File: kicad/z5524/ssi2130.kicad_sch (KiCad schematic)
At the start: 47 parts, among them Q1 2N7002K, U16 SSI2130, U17 DG442xY, U18 TL072, U19 LM311

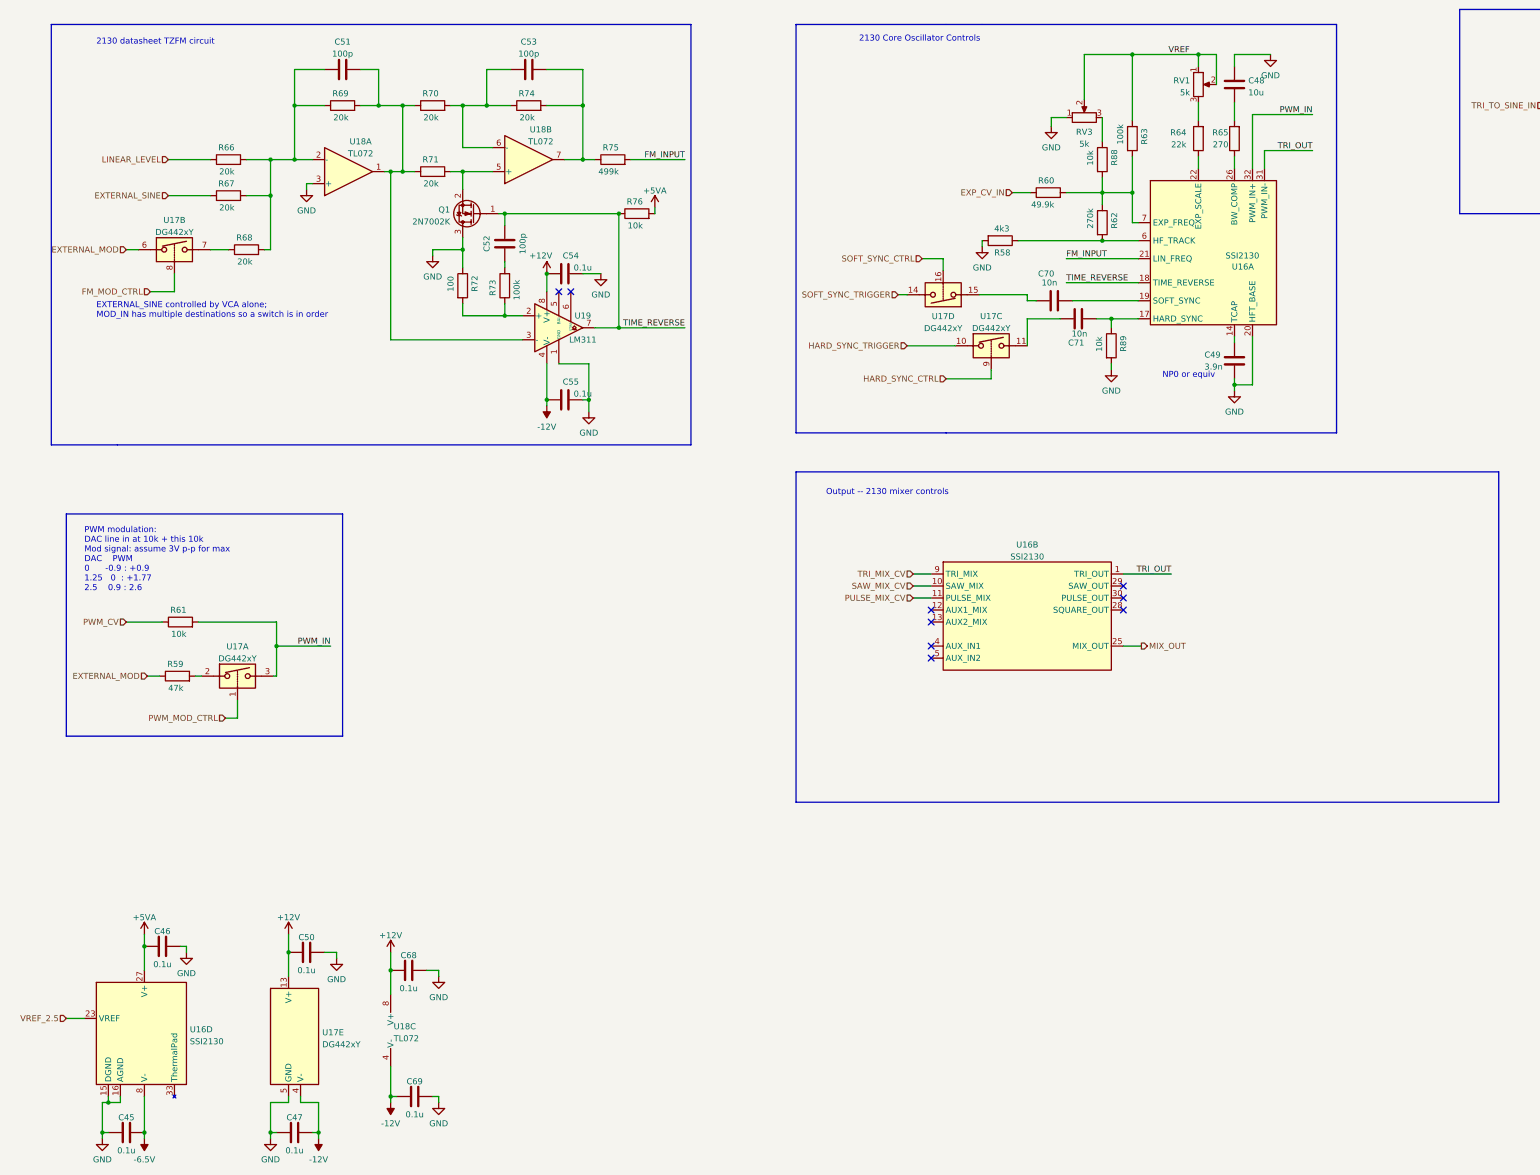
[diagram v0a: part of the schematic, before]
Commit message: calc Vref resistors and fix a couple errors
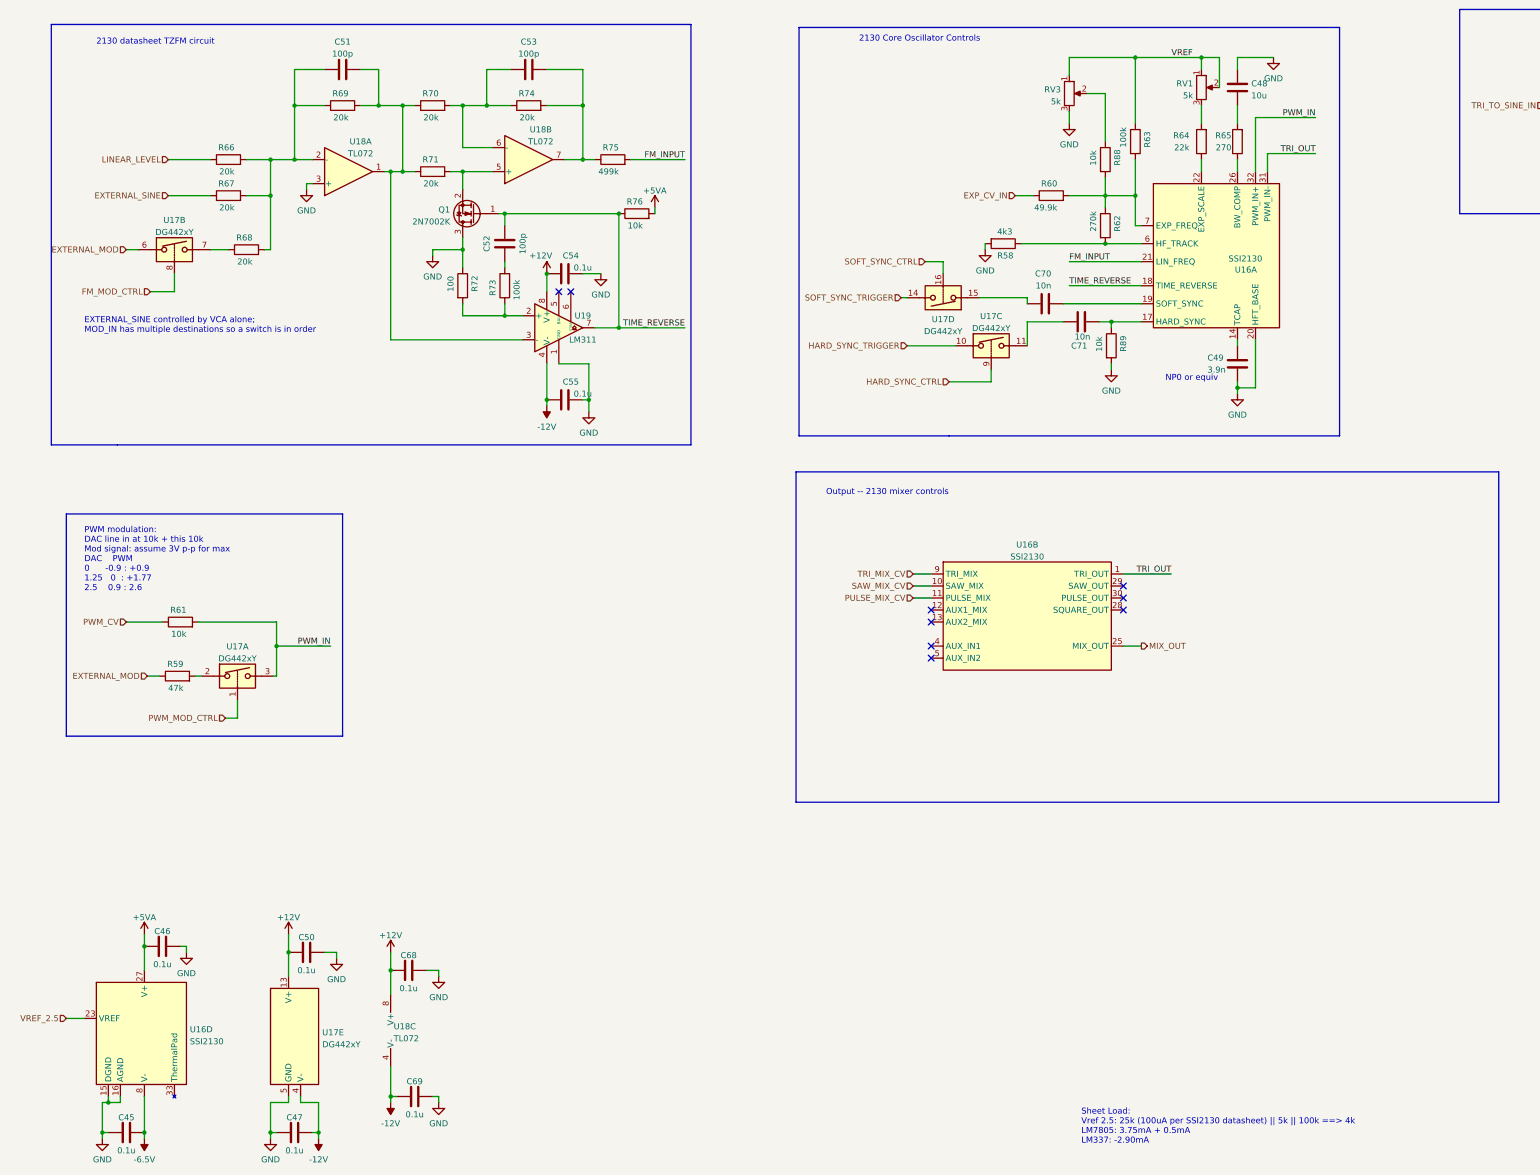
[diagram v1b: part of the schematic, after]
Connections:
- net GND: now also RV3.3; no longer RV3.1
- net VREF: now also RV3.1; no longer RV3.2
- net at R88.1: now also RV3.2; no longer RV3.3
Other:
- note added: "Sheet Load: Vref 2.5: 25k (100uA per SSI2130 datasheet) || 5k || 100k ==> 4k LM7805: 3.75mA + 0.5mA LM337: -2.90mA"
- moved on the sheet: C48, C49, C70, C71, R58, R60, R62, R63, R64, R65, R88, RV1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

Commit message: modify footprint; modify some schematic values
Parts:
- U16: footprint Package_DFN_QFN:QFN-32-1EP_4x4mm_P0.4mm_EP2.65x2.65mm -> Package_DFN_QFN:QFN-32-1EP_4x4mm_P0.4mm_EP2.65x2.65mm_Handsolder
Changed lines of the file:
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@@
     (property "Reference" "U16" (id 0) (at 227.33 127.161 0))
     (property "Value" "SSI2130" (id 1) (at 227.33 129.6979 0))
-    (property "Footprint" "Package_DFN_QFN:QFN-32-1EP_4x4mm_P0.4mm_EP2.65x2.65mm" (id 2) (at 227.33 135.89 0)
+    (property "Footprint" "Package_DFN_QFN:QFN-32-1EP_4x4mm_P0.4mm_EP2.65x2.65mm_Handsolder" (id 2) (at 227.33 135.89 0)
       (effects (font (size 1.27 1.27)) hide)
     )
@@
       (effects (font (size 1.27 1.27)) (justify left))
     )
-    (property "Footprint" "Package_DFN_QFN:QFN-32-1EP_4x4mm_P0.4mm_EP2.65x2.65mm" (id 2) (at 41.91 226.06 0)
+    (property "Footprint" "Package_DFN_QFN:QFN-32-1EP_4x4mm_P0.4mm_EP2.65x2.65mm_Handsolder" (id 2) (at 41.91 226.06 0)
       (effects (font (size 1.27 1.27)) hide)
     )
@@
       (effects (font (size 1.27 1.27)) (justify left))
     )
-    (property "Footprint" "Package_DFN_QFN:QFN-32-1EP_4x4mm_P0.4mm_EP2.65x2.65mm" (id 2) (at 270.51 63.5 0)
+    (property "Footprint" "Package_DFN_QFN:QFN-32-1EP_4x4mm_P0.4mm_EP2.65x2.65mm_Handsolder" (id 2) (at 270.51 63.5 0)
       (effects (font (size 1.27 1.27)) hide)
     )
@@
     (property "Reference" "U16" (id 0) (at 383.54 26.831 0))
     (property "Value" "SSI2130" (id 1) (at 383.54 29.3679 0))
-    (property "Footprint" "Package_DFN_QFN:QFN-32-1EP_4x4mm_P0.4mm_EP2.65x2.65mm" (id 2) (at 384.175 38.1 0)
-      (effects (font (size 1.27 1.27)) hide)
-    )
+    (property "Footprint" "Package_DFN_QFN:QFN-32-1EP_4x4mm_P0.4mm_EP2.65x2.65mm_Handsolder" (id 2) (at 384.175 38.1 0)
+      (effects (font (size 1.27 1.27)) hide)
+    )

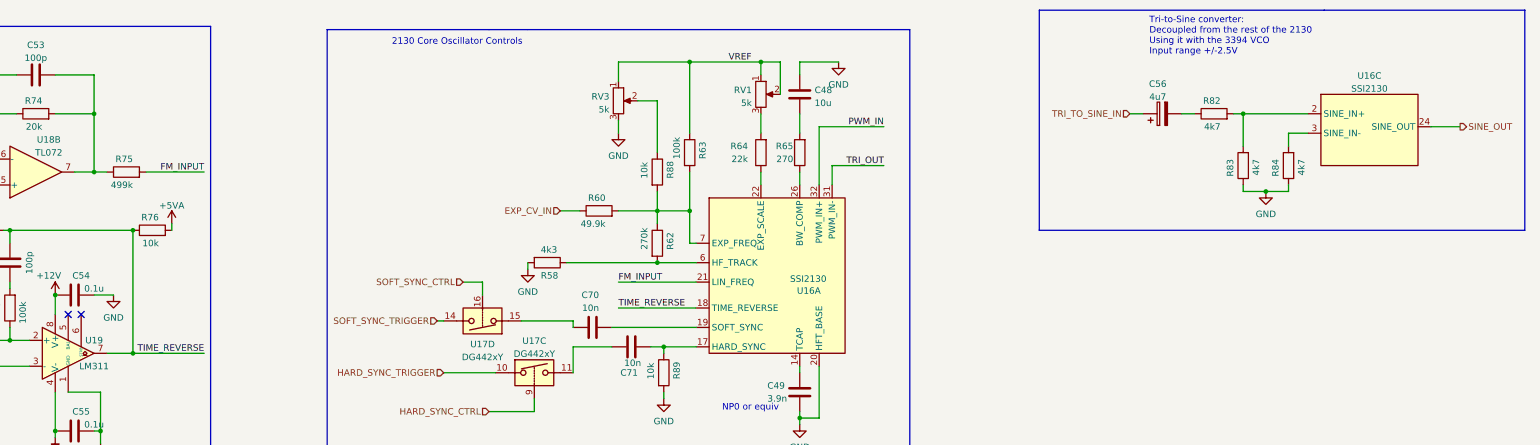
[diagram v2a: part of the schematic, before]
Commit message: further footprint mods; some placement
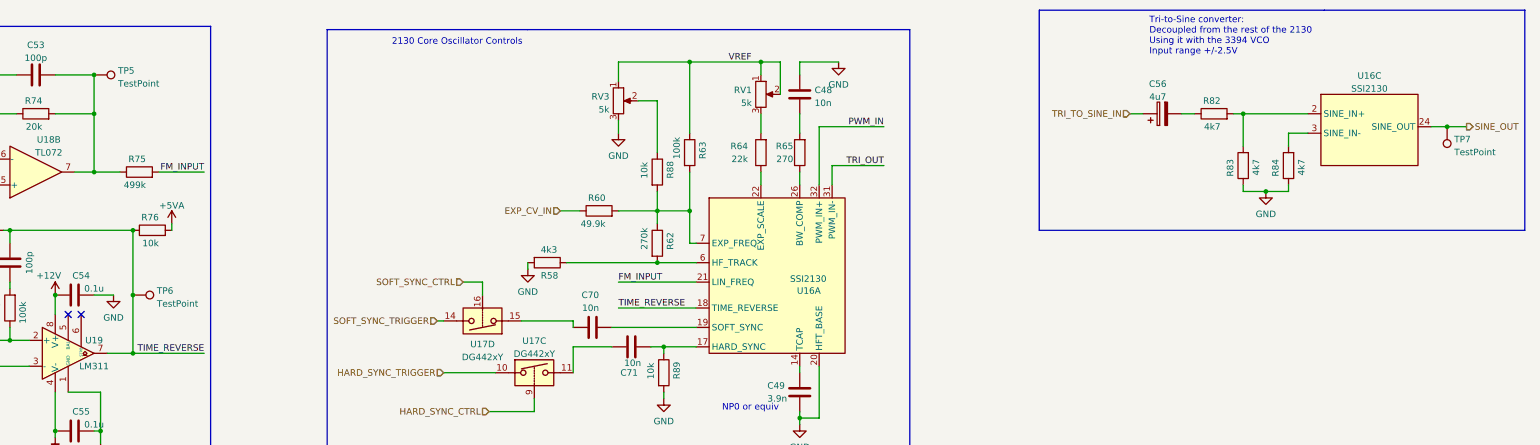
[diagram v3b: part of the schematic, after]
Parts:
- added TP5, TP6, TP7: TestPoint, TestPoint:TestPoint_Pad_1.5x1.5mm, symbol Connector:TestPoint
- C48: value 10u -> 10n; footprint Capacitor_SMD:C_0805_2012Metric -> Capacitor_SMD:C_0603_1608Metric; LCSC Part C15850 -> C57112
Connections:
- net SINE_OUT: now also TP7.1
- net TIME_REVERSE: now also TP6.1
- net at C53.2, R74.2, R75.1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: now also TP5.1
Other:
- moved on the sheet: R75
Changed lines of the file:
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@@
     (company "Zoxnoxious Engineering")
   )
+  (junction (at 398.78 36.83) (diameter 0) (color 0 0 0 0)
+  )
   (junction (at 140.97 57.15) (diameter 0) (color 0 0 0 0)
   )
@@
   (junction (at 92.71 48.26) (diameter 0) (color 0 0 0 0)
   )
+  (junction (at 133.35 26.67) (diameter 0) (color 0 0 0 0)
+  )
   (junction (at 67.31 53.34) (diameter 0) (color 0 0 0 0)
   )
@@
   )
   (junction (at 92.71 243.84) (diameter 0) (color 0 0 0 0)
+  )
+  (junction (at 140.97 69.85) (diameter 0) (color 0 0 0 0)
   )
   (no_connect (at 207.01 151.13))
@@
     (stroke (width 0) (type default) (color 0 0 0 0))
   )
-  (wire (pts (xy 395.605 36.83) (xy 401.32 36.83))
+  (wire (pts (xy 395.605 36.83) (xy 398.78 36.83))
     (stroke (width 0) (type default) (color 0 0 0 0))
   )
@@
     (stroke (width 0) (type default) (color 0 0 0 0))
   )
-  (wire (pts (xy 143.51 45.72) (xy 154.94 45.72))
+  (wire (pts (xy 146.05 45.72) (xy 154.94 45.72))
     (stroke (width 0) (type default) (color 0 0 0 0))
   )
@@
     (stroke (width 0) (type default) (color 0 0 0 0))
   )
+  (wire (pts (xy 140.97 69.85) (xy 140.97 57.15))
+    (stroke (width 0) (type default) (color 0 0 0 0))
+  )
   (wire (pts (xy 107.95 48.26) (xy 107.95 52.07))
     (stroke (width 0) (type default) (color 0 0 0 0))
@@
     (stroke (width 0) (type default) (color 0 0 0 0))
   )
-  (wire (pts (xy 140.97 81.28) (xy 140.97 57.15))
+  (wire (pts (xy 140.97 81.28) (xy 140.97 69.85))
     (stroke (width 0) (type default) (color 0 0 0 0))
   )
@@
     (stroke (width 0) (type default) (color 0 0 0 0))
   )
+  (wire (pts (xy 398.78 36.83) (xy 402.59 36.83))
+    (stroke (width 0) (type default) (color 0 0 0 0))
+  )
   (wire (pts (xy 36.83 64.77) (xy 39.37 64.77))
     (stroke (width 0) (type default) (color 0 0 0 0))
@@
     (stroke (width 0) (type default) (color 0 0 0 0))
   )
-  (wire (pts (xy 133.35 45.72) (xy 135.89 45.72))
-    (stroke (width 0) (type default) (color 0 0 0 0))
-  )
   (wire (pts (xy 74.93 50.8) (xy 74.93 52.07))
     (stroke (width 0) (type default) (color 0 0 0 0))
@@
   )
   (wire (pts (xy 107.95 62.23) (xy 107.95 64.77))
+    (stroke (width 0) (type default) (color 0 0 0 0))
+  )
+  (wire (pts (xy 133.35 45.72) (xy 138.43 45.72))
     (stroke (width 0) (type default) (color 0 0 0 0))
   )
@@
     (effects (font (size 1.27 1.27)) (justify right))
   )
-  (hierarchical_label "SINE_OUT" (shape output) (at 401.32 36.83 0)
+  (hierarchical_label "SINE_OUT" (shape output) (at 402.59 36.83 0)
     (effects (font (size 1.27 1.27)) (justify left))
   )
@@
     (pin "1")
   )
-  (symbol (lib_id "Device:R") (at 139.7 45.72 90) (unit 1)
-    (in_bom yes) (on_board yes)
-    (property "Reference" "R75" (id 0) (at 140.97 43.18 90)
-      (effects (font (size 1.27 1.27)) (justify left))
-    )
-    (property "Value" "499k" (id 1) (at 140.97 48.26 90)
-      (effects (font (size 1.27 1.27)) (justify left))
-    )
-    (property "Footprint" "Resistor_SMD:R_0603_1608Metric" (id 2) (at 139.7 47.498 90)
-      (effects (font (size 1.27 1.27)) hide)
-    )
-    (property "Datasheet" "~" (id 3) (at 139.7 45.72 0)
-      (effects (font (size 1.27 1.27)) hide)
-    )
-    (property "LCSC Part" "" (id 4) (at 139.7 45.72 90)
+  (symbol (lib_id "Connector:TestPoint") (at 140.97 69.85 270) (unit 1)
+    (in_bom yes) (on_board yes) (fields_autoplaced)
+    (property "Reference" "TP6" (id 0) (at 145.669 69.0153 90)
+      (effects (font (size 1.27 1.27)) (justify left))
+    )
+    (property "Value" "TestPoint" (id 1) (at 145.669 71.5522 90)
+      (effects (font (size 1.27 1.27)) (justify left))
+    )
+    (property "Footprint" "TestPoint:TestPoint_Pad_1.5x1.5mm" (id 2) (at 140.97 74.93 0)
+      (effects (font (size 1.27 1.27)) hide)
+    )
+    (property "Datasheet" "~" (id 3) (at 140.97 74.93 0)
+      (effects (font (size 1.27 1.27)) hide)
+    )
+    (pin "1")
+  )
+  (symbol (lib_id "Device:R") (at 142.24 45.72 90) (unit 1)
+    (in_bom yes) (on_board yes)
+    (property "Reference" "R75" (id 0) (at 143.51 43.18 90)
+      (effects (font (size 1.27 1.27)) (justify left))
+    )
+    (property "Value" "499k" (id 1) (at 143.51 48.26 90)
+      (effects (font (size 1.27 1.27)) (justify left))
+    )
+    (property "Footprint" "Resistor_SMD:R_0603_1608Metric" (id 2) (at 142.24 47.498 90)
+      (effects (font (size 1.27 1.27)) hide)
+    )
+    (property "Datasheet" "~" (id 3) (at 142.24 45.72 0)
+      (effects (font (size 1.27 1.27)) hide)
+    )
+    (property "LCSC Part" "" (id 4) (at 142.24 45.72 90)
       (effects (font (size 1.27 1.27)) hide)
     )
@@
       (effects (font (size 1.27 1.27)) (justify left))
     )
-    (property "Value" "10u" (id 1) (at 274.701 32.1822 0)
-      (effects (font (size 1.27 1.27)) (justify left))
-    )
-    (property "Footprint" "Capacitor_SMD:C_0805_2012Metric" (id 2) (at 272.7452 34.29 0)
+    (property "Value" "10n" (id 1) (at 274.701 32.1822 0)
+      (effects (font (size 1.27 1.27)) (justify left))
+    )
+    (property "Footprint" "Capacitor_SMD:C_0603_1608Metric" (id 2) (at 272.7452 34.29 0)
       (effects (font (size 1.27 1.27)) hide)
     )
@@
       (effects (font (size 1.27 1.27)) hide)
     )
-    (property "LCSC Part" "C15850" (id 4) (at 271.78 30.48 0)
+    (property "LCSC Part" "C57112" (id 4) (at 271.78 30.48 0)
       (effects (font (size 1.27 1.27)) hide)
     )
@@
     (pin "2")
   )
+  (symbol (lib_id "Connector:TestPoint") (at 133.35 26.67 270) (unit 1)
+    (in_bom yes) (on_board yes) (fields_autoplaced)
+    (property "Reference" "TP5" (id 0) (at 138.049 25.8353 90)
+      (effects (font (size 1.27 1.27)) (justify left))
+    )
+    (property "Value" "TestPoint" (id 1) (at 138.049 28.3722 90)
+      (effects (font (size 1.27 1.27)) (justify left))
+    )
+    (property "Footprint" "TestPoint:TestPoint_Pad_1.5x1.5mm" (id 2) (at 133.35 31.75 0)
+      (effects (font (size 1.27 1.27)) hide)
+    )
+    (property "Datasheet" "~" (id 3) (at 133.35 31.75 0)
+      (effects (font (size 1.27 1.27)) hide)
+    )
+    (pin "1")
+  )
   (symbol (lib_id "Device:R") (at 367.665 44.45 180) (unit 1)
     (in_bom yes) (on_board yes)
@@
     (pin "2")
   )
+  (symbol (lib_id "Connector:TestPoint") (at 398.78 36.83 180) (unit 1)
+    (in_bom yes) (on_board yes) (fields_autoplaced)
+    (property "Reference" "TP7" (id 0) (at 400.177 39.2973 0)
+      (effects (font (size 1.27 1.27)) (justify right))
+    )
+    (property "Value" "TestPoint" (id 1) (at 400.177 41.8342 0)
+      (effects (font (size 1.27 1.27)) (justify right))
+    )
+    (property "Footprint" "TestPoint:TestPoint_Pad_1.5x1.5mm" (id 2) (at 393.7 36.83 0)
+      (effects (font (size 1.27 1.27)) hide)
+    )
+    (property "Datasheet" "~" (id 3) (at 393.7 36.83 0)
+      (effects (font (size 1.27 1.27)) hide)
+    )
+    (pin "1")
+  )
   (symbol (lib_id "Device:C") (at 129.54 69.85 90) (unit 1)

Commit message: routing coming together...in a bit of a mess
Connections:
- net VREF is gone; now on net VREF_2.5: R63.1, RV1.1, RV1.2, RV3.1
- net HARD_SYNC_CTRL: now also U17.16; no longer U17.9
- net HARD_SYNC_TRIGGER: now also U17.14; no longer U17.10
- net PWM_IN: now also U17.2; no longer U17.3
- net SOFT_SYNC_CTRL: now also U17.9; no longer U17.16
- net SOFT_SYNC_TRIGGER: now also C70.1; no longer U17.14
- net at C71.1: now also U17.15; no longer U17.11
- net at C70.2: now also U17.10; no longer U16.19 (SOFT_SYNC)
- net at R59.2: now also U17.3; no longer U17.2
- new net: U16.19 (SOFT_SYNC), U17.11
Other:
- moved on the sheet: C70, R58, R59, R62, U17A, U17C, U17D

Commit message: more routing
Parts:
- C56: footprint Capacitor_THT:CP_Radial_D4.0mm_P1.50mm -> Capacitor_THT:CP_Radial_D4.0mm_P2.00mm
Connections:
- net FM_VOLTAGE: now reaches C53.2, R74.2, R75.1, TP5.1, U18.7
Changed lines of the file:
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@@
+    (effects (font (size 1.27 1.27)) (justify left bottom))
+  )
+  (label "FM_VOLTAGE" (at 133.35 39.37 0)
     (effects (font (size 1.27 1.27)) (justify left bottom))
   )
@@
     (property "Reference" "C56" (id 0) (at 342.011 28.4312 90))
     (property "Value" "4u7" (id 1) (at 342.011 30.9681 90))
-    (property "Footprint" "Capacitor_THT:CP_Radial_D4.0mm_P1.50mm" (id 2) (at 346.71 33.3248 0)
-      (effects (font (size 1.27 1.27)) hide)
-    )
+    (property "Footprint" "Capacitor_THT:CP_Radial_D4.0mm_P2.00mm" (id 2) (at 346.71 33.3248 0)
+      (effects (font (size 1.27 1.27)) hide)
+    )

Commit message: update to kicad 7
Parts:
- renumbered C52 to C1, C69 to C17, C51 to C19, C54 to C2, C55 to C23, C48 to C27, C47 to C28, C53 to C3, C56 to C31, C46 to C32, C50 to C34, C70 to C37, C71 to C39, C68 to C4, C45 to C6, C49 to C8, R73 to R1, R70 to R16, R69 to R18, R74 to R2, R66 to R22, R68 to R23, R67 to R24, R71 to R28, R72 to R31, R82 to R34, R61 to R36, R83 to R37, R59 to R38, R58 to R39, R88 to R4, R60 to R40, R62 to R41, R84 to R43, R65 to R45, R89 to R49, R76 to R5, R63 to R7, R64 to R8, R75 to R9, RV3 to RV1, RV1 to RV2, TP6 to TP1, TP5 to TP2, TP7 to TP3, U18 to U1, U17 to U13, U16 to U2, U19 to U7
